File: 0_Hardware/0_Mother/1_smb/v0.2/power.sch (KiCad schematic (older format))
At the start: 28 parts, among them P1 CONN_2, P301 CONN_2, U202 LM1117IMP-3.3, U302 MP2562DS

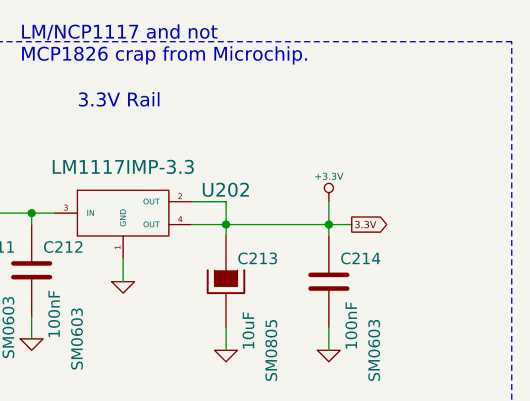
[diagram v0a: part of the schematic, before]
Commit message: mise à jour smb v0.2 (schéma, package, routage). Todo: vérifier les packages des nouveaux composants
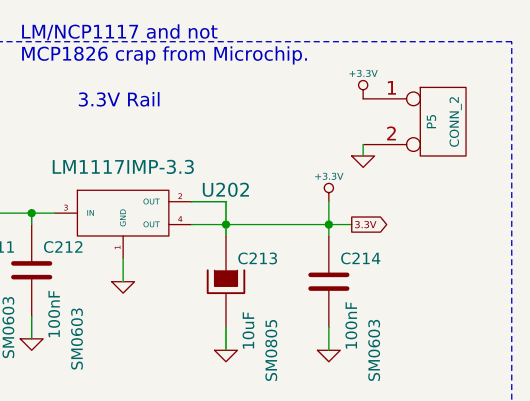
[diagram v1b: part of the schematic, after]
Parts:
- added P5: CONN_2, symbol CONN_2
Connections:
- wire segments 64 -> 65
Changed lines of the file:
@@
 LIBS:ds1340
 LIBS:SMB-cache
-EELAYER 24 0
+EELAYER 27 0
 EELAYER END
 $Descr A4 11693 8268
@@
 Sheet 3 4
 Title "Short Main Board - SMB controler"
-Date "29 jun 2013"
+Date "23 nov 2014"
 Rev "0"
 Comp "XPLDUINO project"
@@
 Self a cabler \nen mode parallele !!!
 $Comp
-L +12V #PWR061
+L +12V #PWR64
 U 1 1 5001A24F
 P 4500 2000
-F 0 "#PWR061" H 4500 1950 20  0001 C CNN
+F 0 "#PWR64" H 4500 1950 20  0001 C CNN
 F 1 "+12V" H 4500 2100 30  0000 C CNN
 F 2 "" H 4500 2000 60  0001 C CNN
@@
 $EndComp
 $Comp
-L GND #PWR062
+L GND #PWR65
 U 1 1 5001A247
 P 4500 2300
-F 0 "#PWR062" H 4500 2300 30  0001 C CNN
+F 0 "#PWR65" H 4500 2300 30  0001 C CNN
 F 1 "GND" H 4500 2230 30  0001 C CNN
 F 2 "" H 4500 2300 60  0001 C CNN
@@
 $EndComp
 $Comp
-L GND #PWR063
+L GND #PWR79
 U 1 1 4FF094DE
 P 8300 3550
-F 0 "#PWR063" H 8300 3550 30  0001 C CNN
+F 0 "#PWR79" H 8300 3550 30  0001 C CNN
 F 1 "GND" H 8300 3480 30  0001 C CNN
 F 2 "" H 8300 3550 60  0001 C CNN
@@
 $EndComp
 $Comp
-L GND #PWR064
+L GND #PWR75
 U 1 1 4FF0947E
 P 6650 2700
-F 0 "#PWR064" H 6650 2700 30  0001 C CNN
+F 0 "#PWR75" H 6650 2700 30  0001 C CNN
 F 1 "GND" H 6650 2630 30  0001 C CNN
 F 2 "" H 6650 2700 60  0001 C CNN
@@
 $EndComp
 $Comp
-L GND #PWR065
+L GND #PWR74
 U 1 1 4FF0947B
 P 6450 2700
-F 0 "#PWR065" H 6450 2700 30  0001 C CNN
+F 0 "#PWR74" H 6450 2700 30  0001 C CNN
 F 1 "GND" H 6450 2630 30  0001 C CNN
 F 2 "" H 6450 2700 60  0001 C CNN
@@
 $EndComp
 $Comp
-L GND #PWR066
+L GND #PWR72
 U 1 1 4FF09478
 P 6250 2700
-F 0 "#PWR066" H 6250 2700 30  0001 C CNN
+F 0 "#PWR72" H 6250 2700 30  0001 C CNN
 F 1 "GND" H 6250 2630 30  0001 C CNN
 F 2 "" H 6250 2700 60  0001 C CNN
@@
 $EndComp
 $Comp
-L GND #PWR067
+L GND #PWR71
 U 1 1 4FF09475
 P 6050 2700
-F 0 "#PWR067" H 6050 2700 30  0001 C CNN
+F 0 "#PWR71" H 6050 2700 30  0001 C CNN
 F 1 "GND" H 6050 2630 30  0001 C CNN
 F 2 "" H 6050 2700 60  0001 C CNN
@@
 $EndComp
 $Comp
-L GND #PWR068
+L GND #PWR69
 U 1 1 4FF09473
 P 5850 2700
-F 0 "#PWR068" H 5850 2700 30  0001 C CNN
+F 0 "#PWR69" H 5850 2700 30  0001 C CNN
 F 1 "GND" H 5850 2630 30  0001 C CNN
 F 2 "" H 5850 2700 60  0001 C CNN
@@
 $EndComp
 $Comp
-L GND #PWR069
+L GND #PWR86
 U 1 1 4FF09319
 P 9100 3550
-F 0 "#PWR069" H 9100 3550 30  0001 C CNN
+F 0 "#PWR86" H 9100 3550 30  0001 C CNN
 F 1 "GND" H 9100 3480 30  0001 C CNN
 F 2 "" H 9100 3550 60  0001 C CNN
@@
 $EndComp
 $Comp
-L GND #PWR070
+L GND #PWR84
 U 1 1 4FF09316
 P 8900 3550
-F 0 "#PWR070" H 8900 3550 30  0001 C CNN
+F 0 "#PWR84" H 8900 3550 30  0001 C CNN
 F 1 "GND" H 8900 3480 30  0001 C CNN
 F 2 "" H 8900 3550 60  0001 C CNN
@@
 $EndComp
 $Comp
-L GND #PWR071
+L GND #PWR81
 U 1 1 4FF09313
 P 8700 3550
-F 0 "#PWR071" H 8700 3550 30  0001 C CNN
+F 0 "#PWR81" H 8700 3550 30  0001 C CNN
 F 1 "GND" H 8700 3480 30  0001 C CNN
 F 2 "" H 8700 3550 60  0001 C CNN
@@
 $EndComp
 $Comp
-L GND #PWR072
+L GND #PWR80
 U 1 1 4FF09310
 P 8500 3550
-F 0 "#PWR072" H 8500 3550 30  0001 C CNN
+F 0 "#PWR80" H 8500 3550 30  0001 C CNN
 F 1 "GND" H 8500 3480 30  0001 C CNN
 F 2 "" H 8500 3550 60  0001 C CNN
@@
 $EndComp
 $Comp
-L +5V #PWR073
+L +5V #PWR76
 U 1 1 4FECCEB6
 P 7050 3300
-F 0 "#PWR073" H 7050 3390 20  0001 C CNN
+F 0 "#PWR76" H 7050 3390 20  0001 C CNN
 F 1 "+5V" H 7050 3390 30  0000 C CNN
 F 2 "" H 7050 3300 60  0001 C CNN
@@
 $EndComp
 $Comp
-L +5V #PWR074
+L +5V #PWR78
 U 1 1 4FECCEAF
 P 8250 3150
-F 0 "#PWR074" H 8250 3240 20  0001 C CNN
+F 0 "#PWR78" H 8250 3240 20  0001 C CNN
 F 1 "+5V" H 8250 3240 30  0000 C CNN
 F 2 "" H 8250 3150 60  0001 C CNN
@@
 $EndComp
 $Comp
-L +12V #PWR075
+L +12V #PWR68
 U 1 1 4FECCB61
 P 5700 2300
-F 0 "#PWR075" H 5700 2250 20  0001 C CNN
+F 0 "#PWR68" H 5700 2250 20  0001 C CNN
 F 1 "+12V" H 5700 2400 30  0000 C CNN
 F 2 "" H 5700 2300 60  0001 C CNN
@@
 $EndComp
 $Comp
-L GND #PWR076
+L GND #PWR66
 U 1 1 4FECC9B9
 P 5000 3500
-F 0 "#PWR076" H 5000 3500 30  0001 C CNN
+F 0 "#PWR66" H 5000 3500 30  0001 C CNN
 F 1 "GND" H 5000 3430 30  0001 C CNN
 F 2 "" H 5000 3500 60  0001 C CNN
@@
 $EndComp
 $Comp
-L GND #PWR077
+L GND #PWR70
 U 1 1 4FECC91D
 P 5950 4650
-F 0 "#PWR077" H 5950 4650 30  0001 C CNN
+F 0 "#PWR70" H 5950 4650 30  0001 C CNN
 F 1 "GND" H 5950 4580 30  0001 C CNN
 F 2 "" H 5950 4650 60  0001 C CNN
@@
 $EndComp
 $Comp
-L GND #PWR078
+L GND #PWR73
 U 1 1 4FECC8D9
 P 6350 3900
-F 0 "#PWR078" H 6350 3900 30  0001 C CNN
+F 0 "#PWR73" H 6350 3900 30  0001 C CNN
 F 1 "GND" H 6350 3830 30  0001 C CNN
 F 2 "" H 6350 3900 60  0001 C CNN
@@
 $EndComp
 $Comp
-L GND #PWR079
+L GND #PWR77
 U 1 1 4FECC83A
 P 7300 3650
-F 0 "#PWR079" H 7300 3650 30  0001 C CNN
+F 0 "#PWR77" H 7300 3650 30  0001 C CNN
 F 1 "GND" H 7300 3580 30  0001 C CNN
 F 2 "" H 7300 3650 60  0001 C CNN
@@
 $EndComp
 $Comp
-L GND #PWR080
+L GND #PWR67
 U 1 1 4FECC725
 P 5400 3900
-F 0 "#PWR080" H 5400 3900 30  0001 C CNN
+F 0 "#PWR67" H 5400 3900 30  0001 C CNN
 F 1 "GND" H 5400 3830 30  0001 C CNN
 F 2 "" H 5400 3900 60  0001 C CNN
@@
 3.3V Rail
 $Comp
-L +5V #PWR081
+L +5V #PWR82
 U 1 1 4FDE4355
 P 8800 1150
-F 0 "#PWR081" H 8800 1240 20  0001 C CNN
+F 0 "#PWR82" H 8800 1240 20  0001 C CNN
 F 1 "+5V" H 8800 1240 30  0000 C CNN
 F 2 "" H 8800 1150 60  0001 C CNN
@@
 $EndComp
 $Comp
-L GND #PWR082
+L GND #PWR83
 U 1 1 4FDE4338
 P 8800 1800
-F 0 "#PWR082" H 8800 1800 30  0001 C CNN
+F 0 "#PWR83" H 8800 1800 30  0001 C CNN
 F 1 "GND" H 8800 1730 30  0001 C CNN
 F 2 "" H 8800 1800 60  0001 C CNN
@@
 $EndComp
 $Comp
-L GND #PWR083
+L GND #PWR85
 U 1 1 4FDE4335
 P 9100 1800
-F 0 "#PWR083" H 9100 1800 30  0001 C CNN
+F 0 "#PWR85" H 9100 1800 30  0001 C CNN
 F 1 "GND" H 9100 1730 30  0001 C CNN
 F 2 "" H 9100 1800 60  0001 C CNN
@@
 $EndComp
 $Comp
-L +3.3V #PWR084
+L +3.3V #PWR89
 U 1 1 4FDE431B
 P 10400 1200
-F 0 "#PWR084" H 10400 1160 30  0001 C CNN
+F 0 "#PWR89" H 10400 1160 30  0001 C CNN
 F 1 "+3.3V" H 10400 1310 30  0000 C CNN
 F 2 "" H 10400 1200 60  0001 C CNN
@@
 $EndComp
 $Comp
-L GND #PWR085
+L GND #PWR90
 U 1 1 4FDE4301
 P 10400 1850
-F 0 "#PWR085" H 10400 1850 30  0001 C CNN
+F 0 "#PWR90" H 10400 1850 30  0001 C CNN
 F 1 "GND" H 10400 1780 30  0001 C CNN
 F 2 "" H 10400 1850 60  0001 C CNN
@@
 $EndComp
 $Comp
-L GND #PWR086
+L GND #PWR88
 U 1 1 4FDE42FD
 P 9950 1850
-F 0 "#PWR086" H 9950 1850 30  0001 C CNN
+F 0 "#PWR88" H 9950 1850 30  0001 C CNN
 F 1 "GND" H 9950 1780 30  0001 C CNN
 F 2 "" H 9950 1850 60  0001 C CNN
@@
 $EndComp
 $Comp
-L GND #PWR087
+L GND #PWR87
 U 1 1 4FDE42B3
 P 9500 1550
-F 0 "#PWR087" H 9500 1550 30  0001 C CNN
+F 0 "#PWR87" H 9500 1550 30  0001 C CNN
 F 1 "GND" H 9500 1480 30  0001 C CNN
 F 2 "" H 9500 1550 60  0001 C CNN
@@
 Text GLabel 10500 1300 2    31   Output ~ 0
 3.3V
+$Comp
+L CONN_2 P5
+U 1 1 54724E4E
+P 10900 850
+F 0 "P5" V 10850 850 40  0000 C CNN
+F 1 "CONN_2" V 10950 850 40  0000 C CNN
+F 2 "" H 10900 850 60  0000 C CNN
+F 3 "" H 10900 850 60  0000 C CNN
+	1    10900 850
+	1    0    0    -1
+$EndComp
+$Comp
+L +3.3V #PWR91
+U 1 1 54724E5B
+P 10550 750
+F 0 "#PWR91" H 10550 710 30  0001 C CNN
+F 1 "+3.3V" H 10550 860 30  0000 C CNN
+F 2 "" H 10550 750 60  0001 C CNN
+F 3 "" H 10550 750 60  0001 C CNN
+	1    10550 750
+	1    0    0    -1
+$EndComp
+$Comp
+L GND #PWR92
+U 1 1 54724E61
+P 10550 1000
+F 0 "#PWR92" H 10550 1000 30  0001 C CNN
+F 1 "GND" H 10550 930 30  0001 C CNN
+F 2 "" H 10550 1000 60  0001 C CNN
+F 3 "" H 10550 1000 60  0001 C CNN
+	1    10550 1000
+	1    0    0    -1
+$EndComp
+Wire Wire Line
+	10550 950  10550 1000
 $EndSCHEMATC
